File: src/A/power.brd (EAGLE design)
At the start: 36 x 88.5 mm, 58 parts, among them CON1 PINHEAD_2X02-0877590414, CON2 PINHEAD_2X02-0877590414, CON3 PINHEAD_2X02-0877590414, CON4 PINHEAD_2X02-0877590414, CON5 PINHEAD_2X02-0877590414, CON6 PINHEAD_2X04-SMD-2-MALE, CON7 PINHEAD_2X02-0877590414, IC1 UCC272-VDFN-HEAVY_PCB, IC2 UCC272-VDFN-HEAVY_PCB, IC3 UCC272-VDFN-HEAVY_PCB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

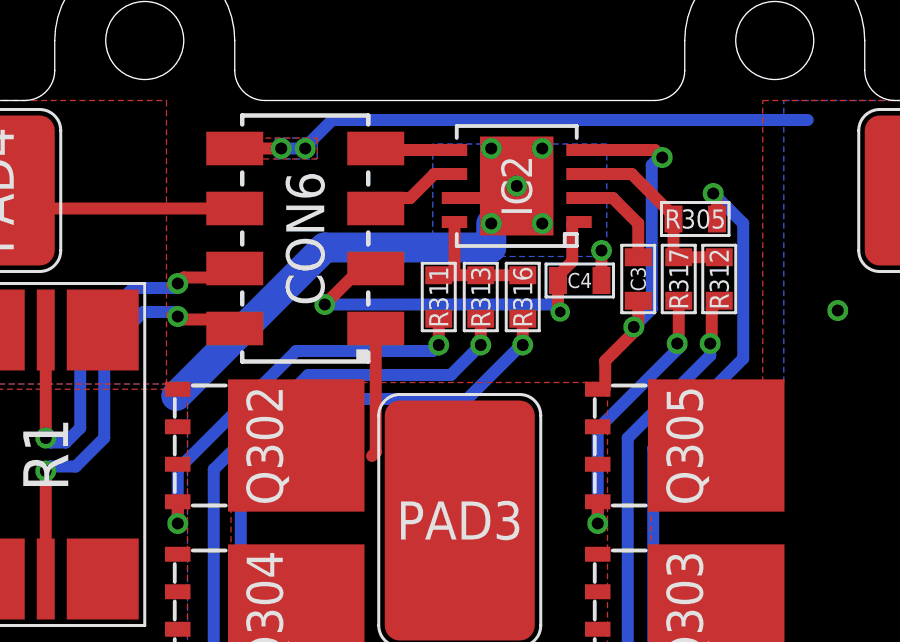
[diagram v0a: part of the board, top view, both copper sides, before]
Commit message: rearrangement and alternate power stage design added
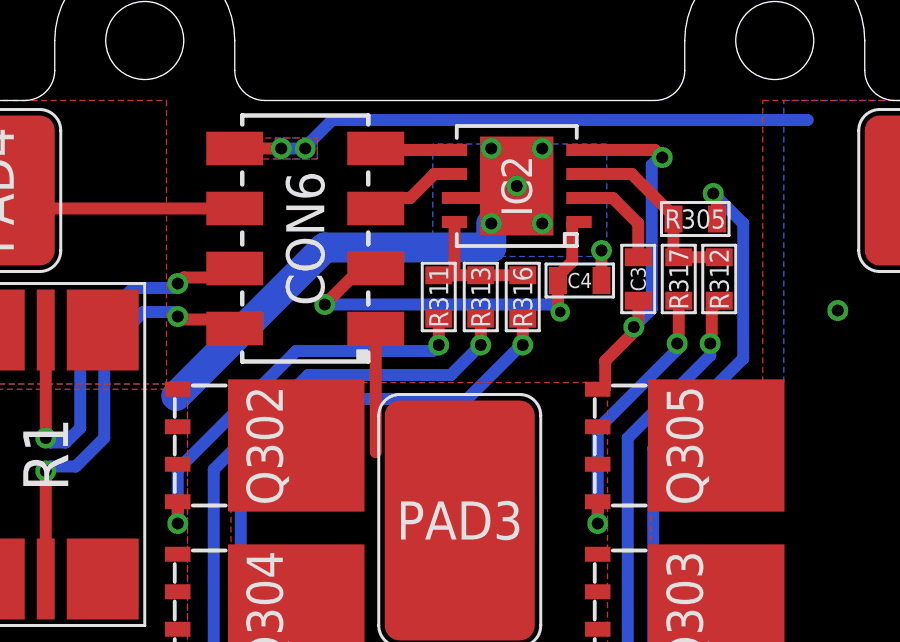
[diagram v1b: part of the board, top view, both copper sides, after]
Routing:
- net PGND: track 28.0 -> 27.5 mm
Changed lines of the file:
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@@
 <setting verticaltext="up"/>
 </settings>
-<grid distance="10" unitdist="mm" unit="mm" style="lines" multiple="1" display="yes" altdistance="1" altunitdist="mm" altunit="mm"/>
+<grid distance="0.1" unitdist="mm" unit="mm" style="lines" multiple="1" display="yes" altdistance="1" altunitdist="mm" altunit="mm"/>
 <layers>
 <layer number="1" name="Top" color="4" fill="1" visible="yes" active="yes"/>
@@
 <layer number="15" name="+3v3" color="4" fill="6" visible="no" active="no"/>
 <layer number="16" name="Bottom" color="1" fill="1" visible="no" active="yes"/>
-<layer number="17" name="Pads" color="2" fill="1" visible="no" active="yes"/>
-<layer number="18" name="Vias" color="2" fill="1" visible="no" active="yes"/>
+<layer number="17" name="Pads" color="2" fill="1" visible="yes" active="yes"/>
+<layer number="18" name="Vias" color="2" fill="1" visible="yes" active="yes"/>
 <layer number="19" name="Unrouted" color="14" fill="1" visible="no" active="yes"/>
-<layer number="20" name="Dimension" color="15" fill="1" visible="no" active="yes"/>
+<layer number="20" name="Dimension" color="15" fill="1" visible="yes" active="yes"/>
 <layer number="21" name="tPlace" color="7" fill="1" visible="yes" active="yes"/>
 <layer number="22" name="bPlace" color="7" fill="1" visible="no" active="yes"/>
@@
 <vertex x="-19" y="0"/>
 </polygon>
-<wire x1="1.9" y1="77.15" x2="2.275" y2="76.775" width="0.4" layer="1"/>
 <wire x1="-0.175" y1="76.75" x2="1.5" y2="76.75" width="0.4" layer="1"/>
 <wire x1="1.5" y1="76.75" x2="1.9" y2="77.15" width="0.4" layer="1"/>
@@
 <contactref element="CON6" pad="1"/>
 <wire x1="-2.8" y1="72.4" x2="-2.8" y2="68.275" width="0.4" layer="1"/>
-<wire x1="-2.8" y1="68.275" x2="-2.925" y2="68.15" width="0.4" layer="1"/>
 </signal>
 <signal name="C_GL">
